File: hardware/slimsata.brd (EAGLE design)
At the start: 16.9 x 80 mm, 2 parts

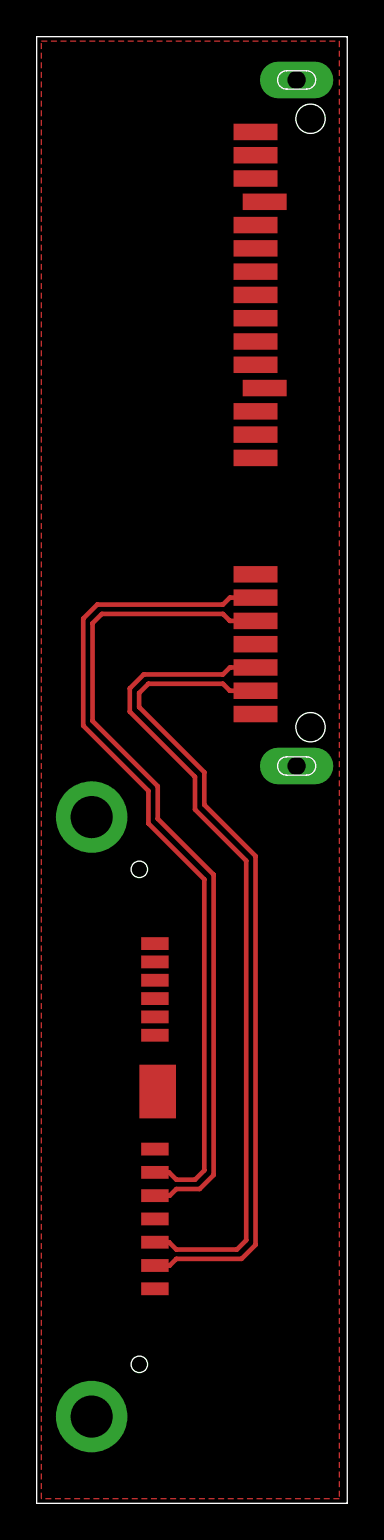
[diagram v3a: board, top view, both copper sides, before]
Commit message: bei Variante 1 Versorgung geroutet
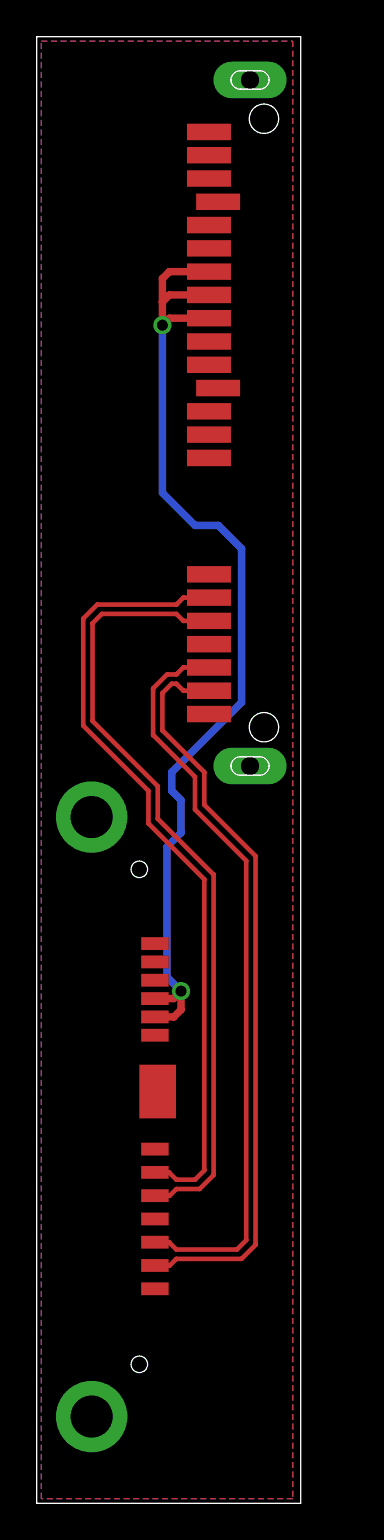
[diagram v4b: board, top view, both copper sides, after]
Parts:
- moved CON1 2.54 mm to (14.5, 58.9)
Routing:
- net N$3: track 0.00 -> 56.1 mm, vias 0 -> 2
- net N$5: track 45.4 -> 41.1 mm
- net N$6: track 45.4 -> 41.1 mm
- net N$8: track 45.8 -> 43.2 mm
- net N$7: track 45.8 -> 43.2 mm
- added copper zone on layer 16, net GND
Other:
- board size 16.9 x 80 mm -> 14.4 x 80 mm
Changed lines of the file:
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@@
 <board>
 <plain>
-<wire x1="0" y1="0" x2="16.942" y2="0" width="0" layer="20"/>
-<wire x1="16.942" y1="0" x2="16.942" y2="80" width="0" layer="20"/>
-<wire x1="16.942" y1="80" x2="0" y2="80" width="0" layer="20"/>
+<wire x1="0" y1="0" x2="14.402" y2="0" width="0" layer="20"/>
+<wire x1="14.402" y1="0" x2="14.402" y2="80" width="0" layer="20"/>
+<wire x1="14.402" y1="80" x2="0" y2="80" width="0" layer="20"/>
 <wire x1="0" y1="80" x2="0" y2="0" width="0" layer="20"/>
 </plain>
@@
 </autorouter>
 <elements>
-<element name="CON1" library="sata" package="MOLEX_47018" value="" x="17.018" y="58.928" rot="R90"/>
+<element name="CON1" library="sata" package="MOLEX_47018" value="" x="14.478" y="58.928" rot="R90"/>
 <element name="CON2" library="sata" package="MOLEX_47300-1005" value="" x="0" y="21.082" rot="R270"/>
 </elements>
@@
 <wire x1="11.938" y1="14.097" x2="11.938" y2="35.306" width="0.254" layer="1"/>
 <wire x1="11.938" y1="35.306" x2="9.144" y2="38.1" width="0.254" layer="1"/>
-<wire x1="5.588" y1="44.196" x2="5.588" y2="43.434" width="0.254" layer="1"/>
-<wire x1="9.144" y1="39.878" x2="5.588" y2="43.434" width="0.254" layer="1"/>
+<wire x1="6.858" y1="44.196" x2="6.858" y2="42.164" width="0.254" layer="1"/>
+<wire x1="9.144" y1="39.878" x2="6.858" y2="42.164" width="0.254" layer="1"/>
 <wire x1="9.144" y1="39.878" x2="9.144" y2="38.1" width="0.254" layer="1"/>
-<wire x1="11.938" y1="44.323" x2="10.541" y2="44.323" width="0.254" layer="1"/>
-<wire x1="10.541" y1="44.323" x2="10.16" y2="44.704" width="0.254" layer="1"/>
-<wire x1="10.16" y1="44.704" x2="6.096" y2="44.704" width="0.254" layer="1"/>
-<wire x1="6.096" y1="44.704" x2="5.588" y2="44.196" width="0.254" layer="1"/>
+<wire x1="9.398" y1="44.323" x2="8.001" y2="44.323" width="0.254" layer="1"/>
+<wire x1="8.001" y1="44.323" x2="7.62" y2="44.704" width="0.254" layer="1"/>
+<wire x1="7.62" y1="44.704" x2="7.366" y2="44.704" width="0.254" layer="1"/>
+<wire x1="7.366" y1="44.704" x2="6.858" y2="44.196" width="0.254" layer="1"/>
 </signal>
 <signal name="N$6">
@@
 <wire x1="11.43" y1="14.351" x2="11.43" y2="35.052" width="0.254" layer="1"/>
 <wire x1="11.43" y1="35.052" x2="8.636" y2="37.846" width="0.254" layer="1"/>
-<wire x1="5.08" y1="43.18" x2="5.08" y2="44.45" width="0.254" layer="1"/>
-<wire x1="5.08" y1="43.18" x2="8.636" y2="39.624" width="0.254" layer="1"/>
+<wire x1="6.35" y1="41.91" x2="6.35" y2="44.45" width="0.254" layer="1"/>
+<wire x1="6.35" y1="41.91" x2="8.636" y2="39.624" width="0.254" layer="1"/>
 <wire x1="8.636" y1="39.624" x2="8.636" y2="37.846" width="0.254" layer="1"/>
-<wire x1="11.938" y1="45.593" x2="10.541" y2="45.593" width="0.254" layer="1"/>
-<wire x1="10.541" y1="45.593" x2="10.16" y2="45.212" width="0.254" layer="1"/>
-<wire x1="10.16" y1="45.212" x2="5.842" y2="45.212" width="0.254" layer="1"/>
-<wire x1="5.842" y1="45.212" x2="5.08" y2="44.45" width="0.254" layer="1"/>
+<wire x1="9.398" y1="45.593" x2="8.001" y2="45.593" width="0.254" layer="1"/>
+<wire x1="8.001" y1="45.593" x2="7.62" y2="45.212" width="0.254" layer="1"/>
+<wire x1="7.62" y1="45.212" x2="7.112" y2="45.212" width="0.254" layer="1"/>
+<wire x1="7.112" y1="45.212" x2="6.35" y2="44.45" width="0.254" layer="1"/>
 </signal>
 <signal name="N$7">
@@
 <wire x1="3.048" y1="42.672" x2="6.604" y2="39.116" width="0.254" layer="1"/>
 <wire x1="6.604" y1="39.116" x2="6.604" y2="37.338" width="0.254" layer="1"/>
-<wire x1="11.938" y1="48.133" x2="10.541" y2="48.133" width="0.254" layer="1"/>
-<wire x1="10.541" y1="48.133" x2="10.16" y2="48.514" width="0.254" layer="1"/>
-<wire x1="10.16" y1="48.514" x2="3.556" y2="48.514" width="0.254" layer="1"/>
+<wire x1="9.398" y1="48.133" x2="8.001" y2="48.133" width="0.254" layer="1"/>
+<wire x1="8.001" y1="48.133" x2="7.62" y2="48.514" width="0.254" layer="1"/>
+<wire x1="7.62" y1="48.514" x2="3.556" y2="48.514" width="0.254" layer="1"/>
 </signal>
 <signal name="N$8">
@@
 <wire x1="2.54" y1="42.418" x2="6.096" y2="38.862" width="0.254" layer="1"/>
 <wire x1="6.096" y1="38.862" x2="6.096" y2="37.084" width="0.254" layer="1"/>
-<wire x1="11.938" y1="49.403" x2="10.541" y2="49.403" width="0.254" layer="1"/>
-<wire x1="10.541" y1="49.403" x2="10.16" y2="49.022" width="0.254" layer="1"/>
-<wire x1="10.16" y1="49.022" x2="3.302" y2="49.022" width="0.254" layer="1"/>
+<wire x1="9.398" y1="49.403" x2="8.001" y2="49.403" width="0.254" layer="1"/>
+<wire x1="8.001" y1="49.403" x2="7.62" y2="49.022" width="0.254" layer="1"/>
+<wire x1="7.62" y1="49.022" x2="3.302" y2="49.022" width="0.254" layer="1"/>
 </signal>
 <signal name="N$3">
@@
 <contactref element="CON2" pad="P2"/>
 <contactref element="CON2" pad="P3"/>
-<wire x1="11.938" y1="65.913" x2="11.938" y2="67.183" width="0" layer="19" extent="1-1"/>
-<wire x1="11.938" y1="64.643" x2="11.938" y2="65.913" width="0" layer="19" extent="1-1"/>
-<wire x1="6.45" y1="27.532" x2="11.938" y2="64.643" width="0" layer="19" extent="1-1"/>
-<wire x1="6.45" y1="26.532" x2="6.45" y2="27.532" width="0" layer="19" extent="1-1"/>
+<wire x1="6.45" y1="26.532" x2="7.482" y2="26.532" width="0.4064" layer="1"/>
+<wire x1="7.482" y1="26.532" x2="7.874" y2="26.924" width="0.4064" layer="1"/>
+<wire x1="6.45" y1="27.532" x2="7.466" y2="27.532" width="0.4064" layer="1"/>
+<wire x1="7.466" y1="27.532" x2="7.874" y2="27.94" width="0.4064" layer="1"/>
+<via x="7.874" y="27.94" extent="1-16" drill="0.6"/>
+<wire x1="7.874" y1="27.94" x2="7.112" y2="28.702" width="0.4064" layer="16"/>
+<wire x1="7.112" y1="28.702" x2="7.112" y2="35.814" width="0.4064" layer="16"/>
+<wire x1="7.112" y1="35.814" x2="7.874" y2="36.576" width="0.4064" layer="16"/>
+<wire x1="7.874" y1="36.576" x2="7.874" y2="38.354" width="0.4064" layer="16"/>
+<wire x1="7.874" y1="38.354" x2="7.366" y2="38.862" width="0.4064" layer="16"/>
+<wire x1="7.366" y1="38.862" x2="7.366" y2="39.878" width="0.4064" layer="16"/>
+<wire x1="7.366" y1="39.878" x2="11.176" y2="43.688" width="0.4064" layer="16"/>
+<wire x1="11.176" y1="43.688" x2="11.176" y2="52.07" width="0.4064" layer="16"/>
+<wire x1="11.176" y1="52.07" x2="9.906" y2="53.34" width="0.4064" layer="16"/>
+<wire x1="9.906" y1="53.34" x2="8.636" y2="53.34" width="0.4064" layer="16"/>
+<wire x1="8.636" y1="53.34" x2="6.858" y2="55.118" width="0.4064" layer="16"/>
+<wire x1="6.858" y1="55.118" x2="6.858" y2="64.262" width="0.4064" layer="16"/>
+<wire x1="9.398" y1="64.643" x2="7.239" y2="64.643" width="0.4064" layer="1"/>
+<wire x1="7.239" y1="64.643" x2="6.858" y2="64.262" width="0.4064" layer="1"/>
+<wire x1="9.398" y1="65.913" x2="7.239" y2="65.913" width="0.4064" layer="1"/>
+<wire x1="7.239" y1="65.913" x2="6.858" y2="65.532" width="0.4064" layer="1"/>
+<wire x1="6.858" y1="65.532" x2="6.858" y2="64.262" width="0.4064" layer="1"/>
+<wire x1="9.398" y1="67.183" x2="7.239" y2="67.183" width="0.4064" layer="1"/>
+<wire x1="7.239" y1="67.183" x2="6.858" y2="66.802" width="0.4064" layer="1"/>
+<wire x1="6.858" y1="66.802" x2="6.858" y2="65.532" width="0.4064" layer="1"/>
+<via x="6.858" y="64.262" extent="1-16" drill="0.6"/>
+<wire x1="7.874" y1="26.924" x2="7.874" y2="27.94" width="0.4064" layer="1"/>
 </signal>
 <signal name="GND">
@@
 <polygon width="0.4064" layer="1">
 <vertex x="0.254" y="79.756"/>
-<vertex x="16.51" y="79.756"/>
-<vertex x="16.51" y="0.254"/>
+<vertex x="13.97" y="79.756"/>
+<vertex x="13.97" y="0.254"/>
 <vertex x="0.254" y="0.254"/>
 </polygon>
-<wire x1="12.438" y1="70.993" x2="14.178" y2="77.638" width="0" layer="19" extent="1-1"/>
-<wire x1="11.938" y1="68.453" x2="12.438" y2="70.993" width="0" layer="19" extent="1-1"/>
-<wire x1="11.938" y1="63.373" x2="11.938" y2="68.453" width="0" layer="19" extent="1-1"/>
-<wire x1="11.938" y1="62.103" x2="11.938" y2="63.373" width="0" layer="19" extent="1-1"/>
-<wire x1="12.438" y1="60.833" x2="11.938" y2="62.103" width="0" layer="19" extent="1-1"/>
-<wire x1="11.938" y1="50.673" x2="12.438" y2="60.833" width="0" layer="19" extent="1-1"/>
-<wire x1="11.938" y1="46.863" x2="11.938" y2="50.673" width="0" layer="19" extent="1-1"/>
-<wire x1="11.938" y1="43.053" x2="11.938" y2="46.863" width="0" layer="19" extent="1-1"/>
-<wire x1="14.178" y1="40.218" x2="11.938" y2="43.053" width="0" layer="19" extent="1-1"/>
-<wire x1="3" y1="37.432" x2="11.938" y2="43.053" width="0" layer="19" extent="1-1"/>
-<wire x1="6.45" y1="30.532" x2="3" y2="37.432" width="0" layer="19" extent="1-1"/>
-<wire x1="6.45" y1="29.532" x2="6.45" y2="30.532" width="0" layer="19" extent="1-1"/>
-<wire x1="6.6" y1="22.462" x2="6.45" y2="29.532" width="0" layer="19" extent="1-1"/>
-<wire x1="6.45" y1="19.322" x2="6.6" y2="22.462" width="0" layer="19" extent="1-1"/>
-<wire x1="6.45" y1="15.512" x2="6.45" y2="19.322" width="0" layer="19" extent="1-1"/>
-<wire x1="6.45" y1="11.702" x2="6.45" y2="15.512" width="0" layer="19" extent="1-1"/>
-<wire x1="3" y1="4.732" x2="6.45" y2="11.702" width="0" layer="19" extent="1-1"/>
+<polygon width="0.4064" layer="16">
+<vertex x="0.254" y="79.756"/>
+<vertex x="13.97" y="79.756"/>
+<vertex x="13.97" y="0.254"/>
+<vertex x="0.254" y="0.254"/>
+</polygon>
 </signal>
 </signals>

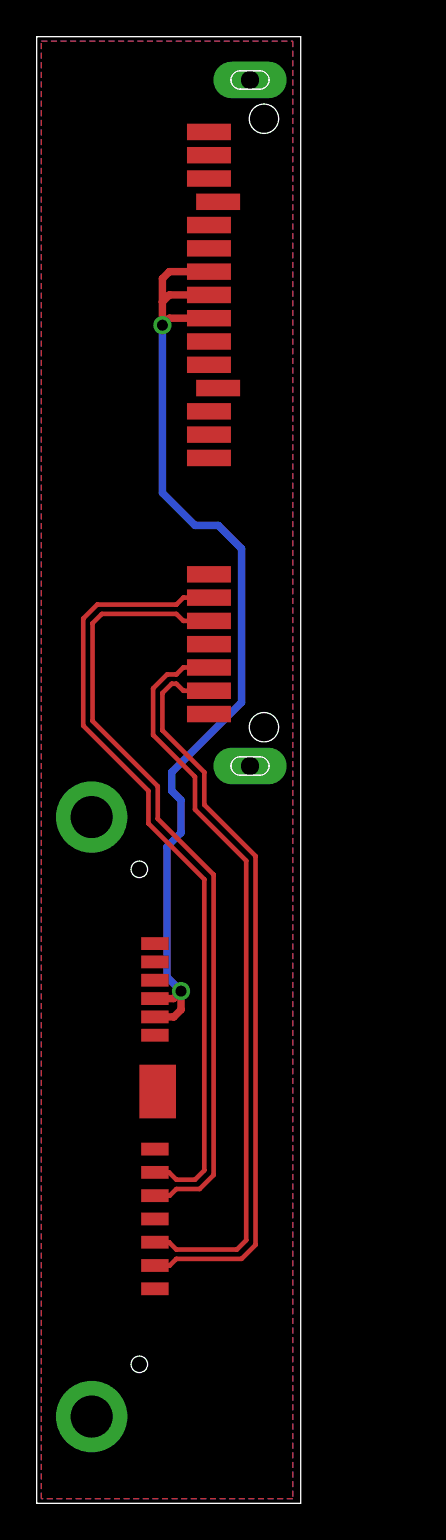
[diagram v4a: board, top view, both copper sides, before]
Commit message: Stecker Molex 67492 platziert, Platinenumrisse angepasst
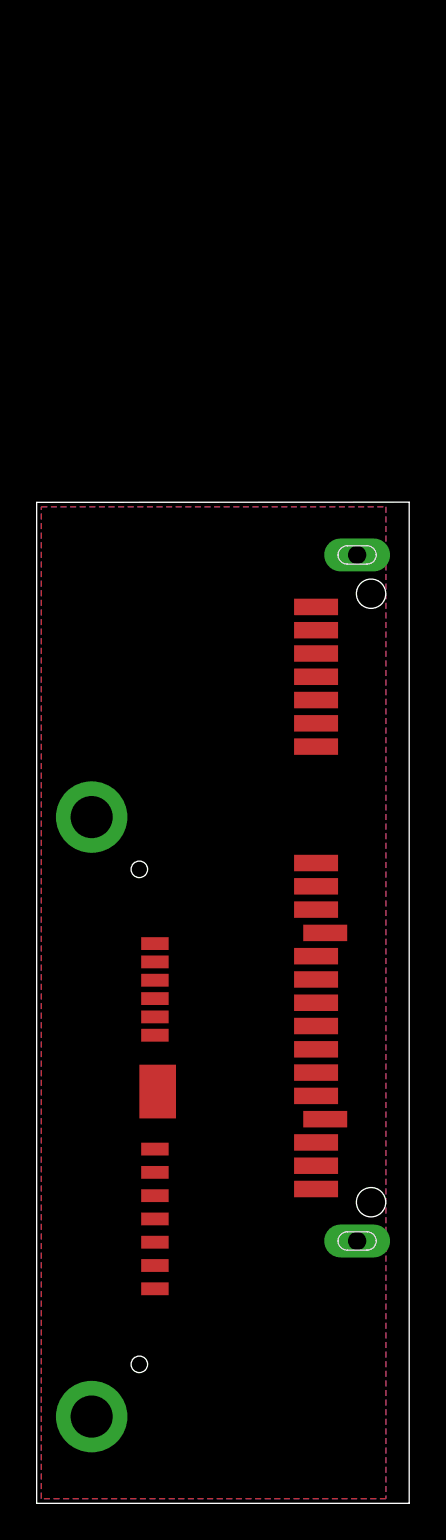
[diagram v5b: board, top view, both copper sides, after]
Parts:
- CON1: value (none) -> MOLEX_67492; device sata:MOLEX_47018 -> sata:MOLEX_67492
- moved CON1 26.6 mm to (20.3, 33.0)
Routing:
- net N$3: track 56.1 -> 0.00 mm, vias 2 -> 0
- net N$8: track 43.2 -> 0.00 mm
- net N$7: track 43.2 -> 0.00 mm
- net N$6: track 41.1 -> 0.00 mm
- net N$5: track 41.1 -> 0.00 mm
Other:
- board size 14.4 x 80 mm -> 20.3 x 54.6 mm
